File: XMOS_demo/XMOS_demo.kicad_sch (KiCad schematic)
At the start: 13 parts

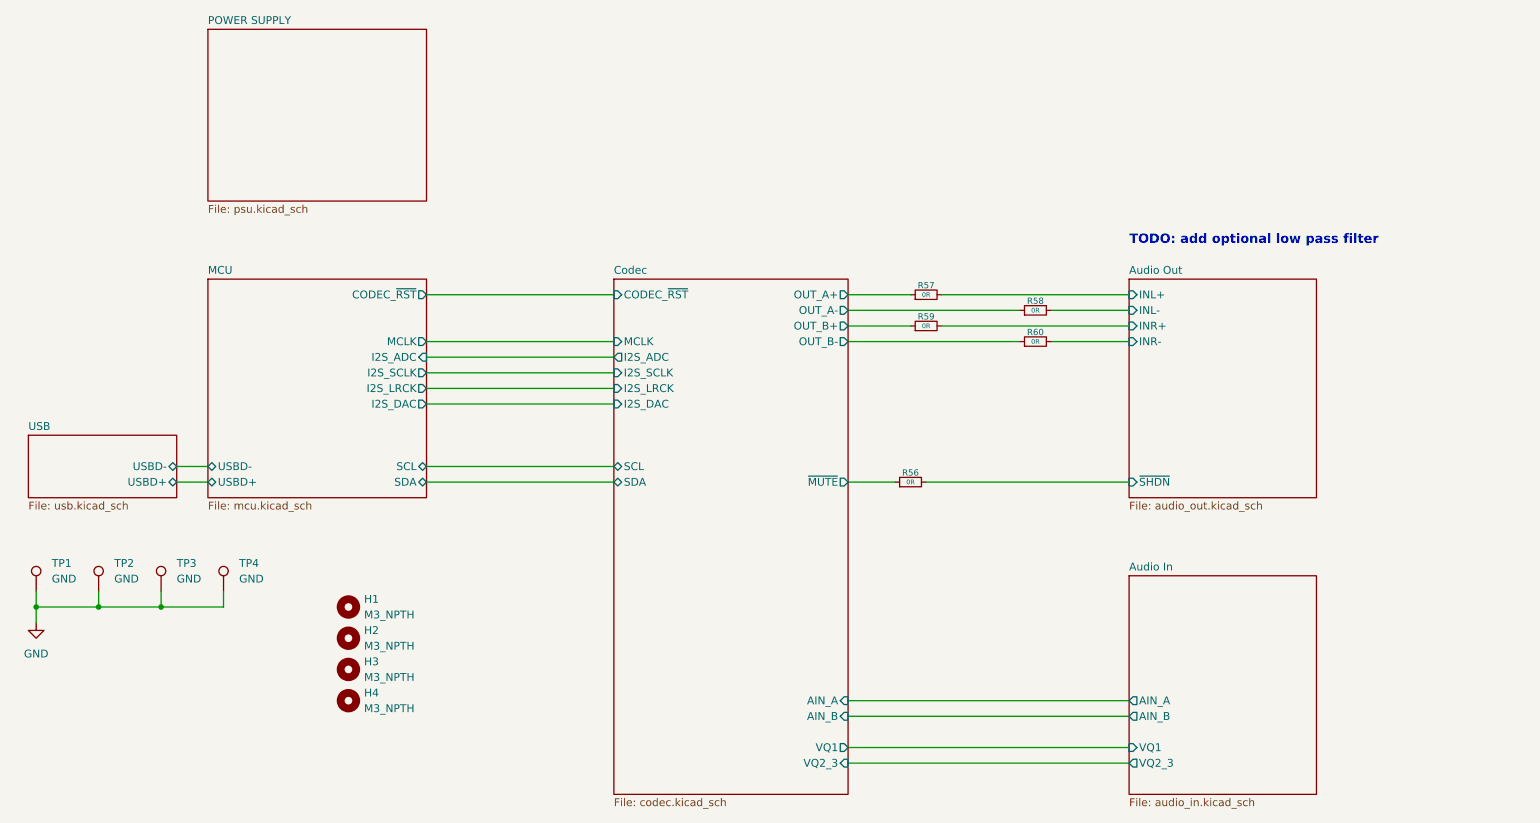
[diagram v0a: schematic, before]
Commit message: I2S config sch page added
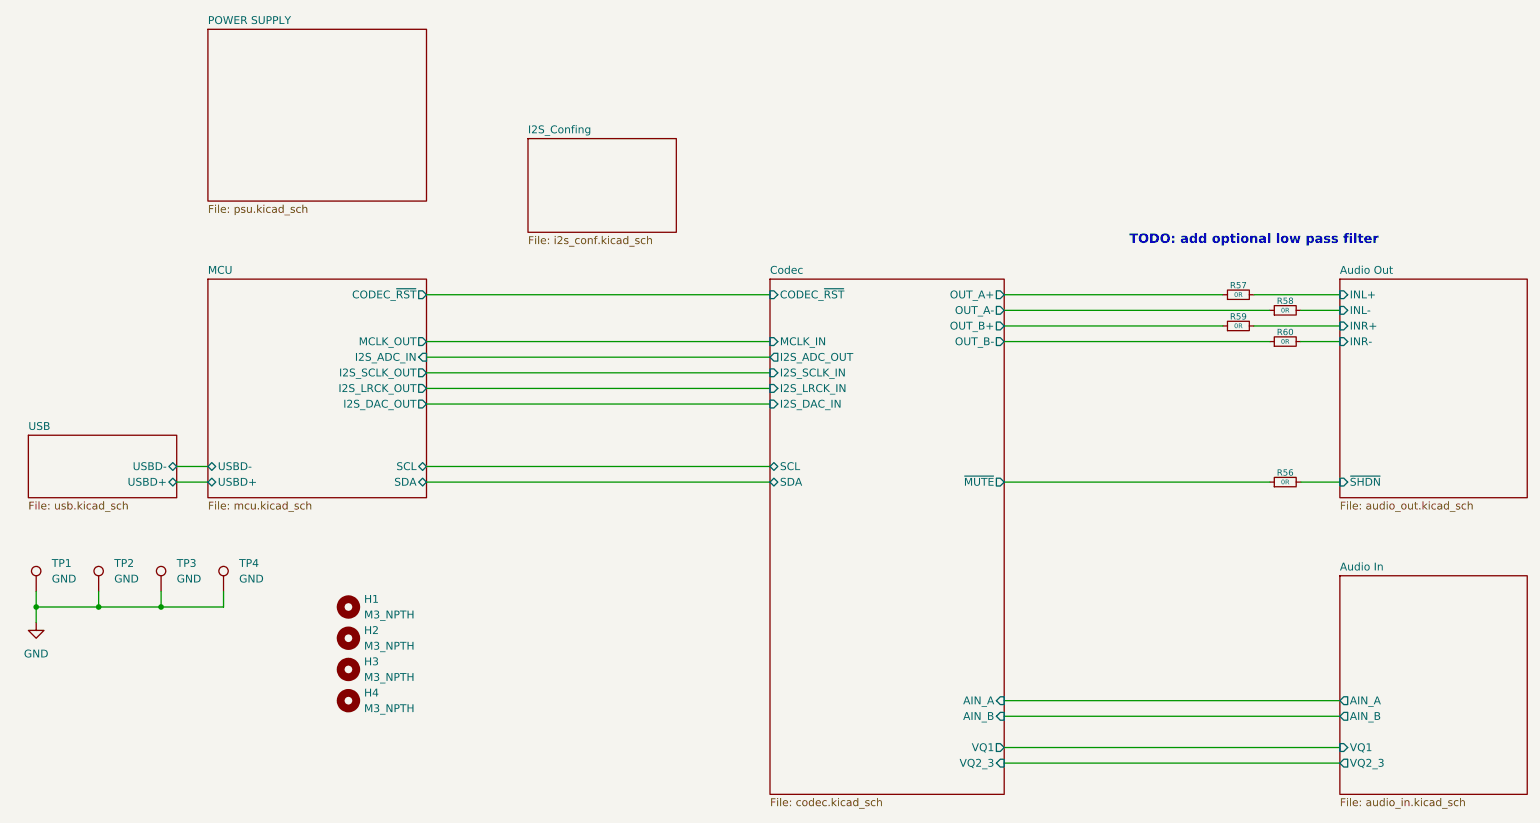
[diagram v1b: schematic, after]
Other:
- added sheet I2S_Confing (i2s_conf.kicad_sch)
- sheet Codec ports: added I2S_ADC_OUT, I2S_DAC_IN, I2S_LRCK_IN, I2S_SCLK_IN, MCLK_IN; removed I2S_ADC, I2S_DAC, I2S_LRCK, I2S_SCLK, MCLK
- sheet MCU ports: added I2S_ADC_IN, I2S_DAC_OUT, I2S_LRCK_OUT, I2S_SCLK_OUT, MCLK_OUT; removed I2S_ADC, I2S_DAC, I2S_LRCK, I2S_SCLK, MCLK
- moved on the sheet: R56, R57, R58, R59, R60

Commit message: Summary (required)
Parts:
- renumbered R57 to R1, R58 to R2, R59 to R3, R60 to R4, R56 to R5
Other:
- sheet I2S_Confing ports: added I2S_ADC_IN, I2S_ADC_OUT, I2S_DAC_IN, I2S_DAC_OUT, I2S_LRCK_IN, I2S_LRCK_OUT, I2S_SCLK_IN, I2S_SCLK_OUT, MCLK_IN, MCLK_OUT; removed none

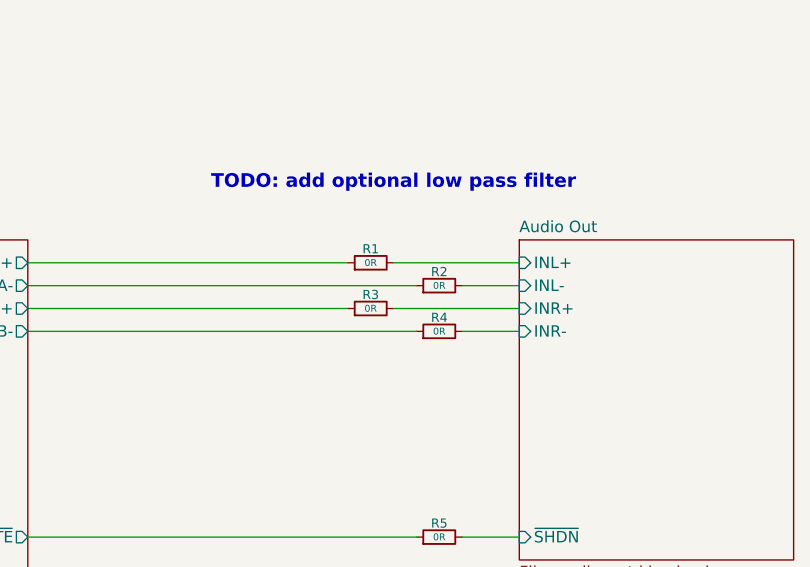
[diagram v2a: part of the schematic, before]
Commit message: Started changes on power supply (audio in) on schematic
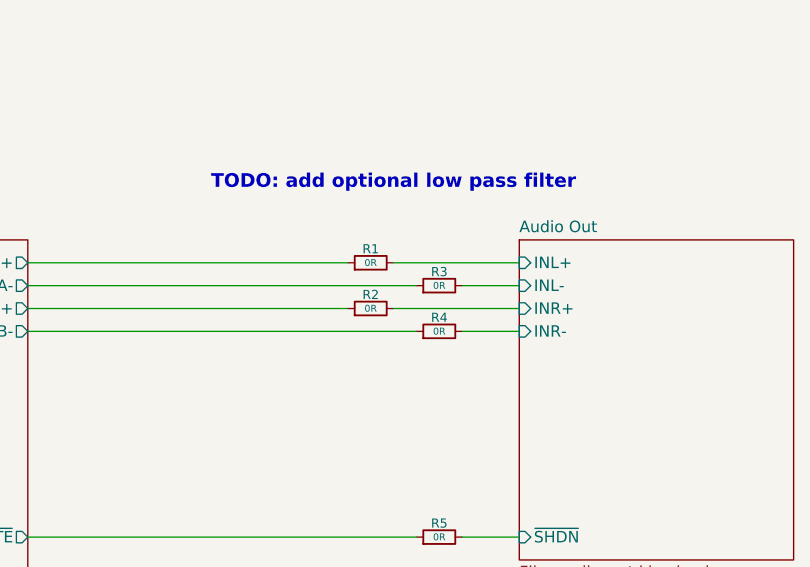
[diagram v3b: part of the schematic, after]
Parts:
- renumbered R3 to R2, R2 to R3
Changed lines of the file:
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@@
 		(on_board yes)
 		(dnp no)
-		(property "Reference" "R3"
+		(property "Reference" "R2"
 			(at 231.14 82.296 90)
 			(effects
@@
 			(project "XMOS_demo"
 				(path "/0a855fb0-ca19-4770-811e-70d8770d7fdd"
-					(reference "R3")
+					(reference "R2")
 					(unit 1)
 				)
@@
 		(on_board yes)
 		(dnp no)
-		(property "Reference" "R2"
+		(property "Reference" "R3"
 			(at 238.76 79.756 90)
 			(effects
@@
 			(project "XMOS_demo"
 				(path "/0a855fb0-ca19-4770-811e-70d8770d7fdd"
-					(reference "R2")
-					(unit 1)
-				)
+					(reference "R3")
+					(unit 1)
+				)

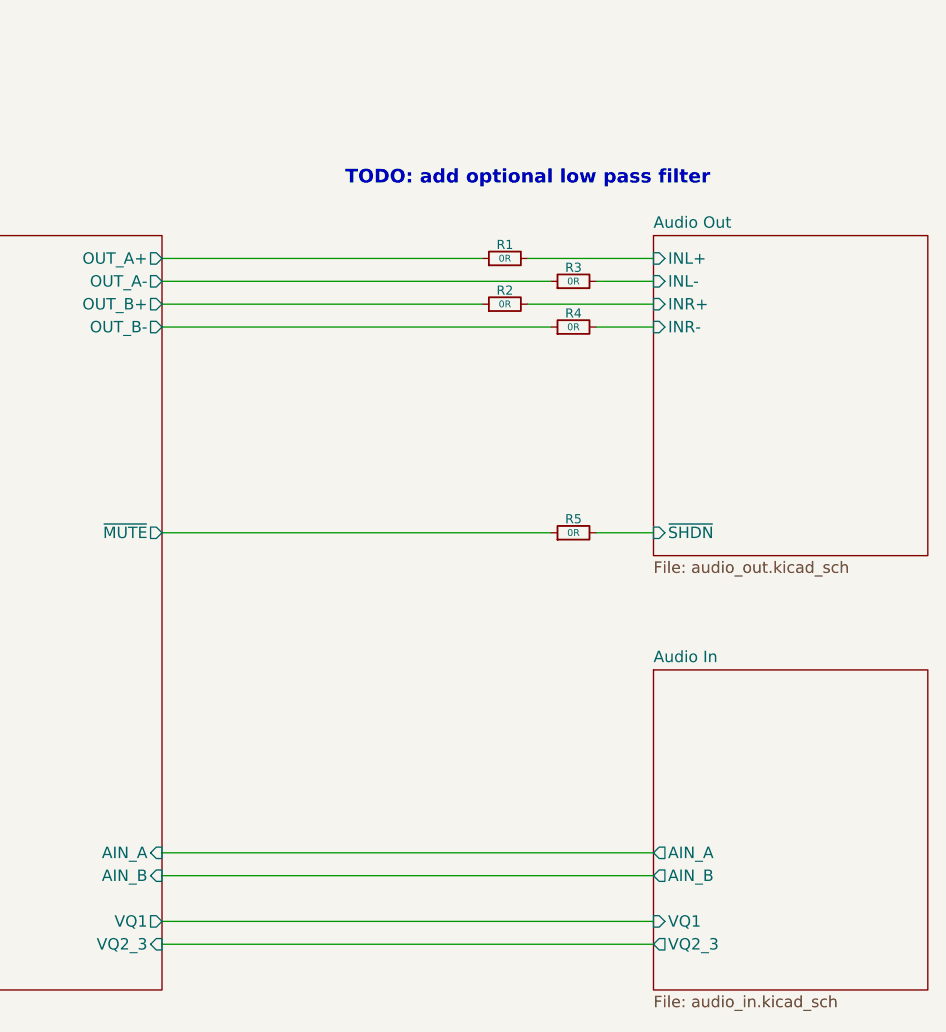
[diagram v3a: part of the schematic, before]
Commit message: Passive lpf added to autio output
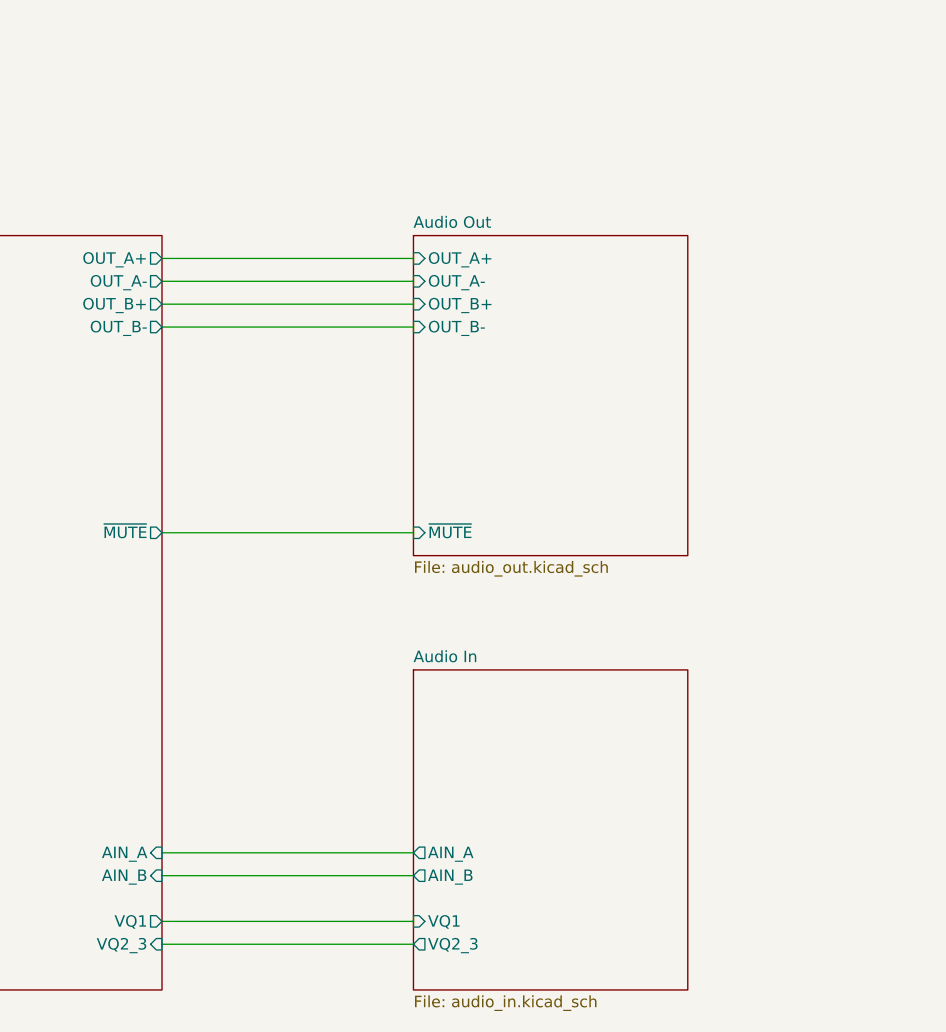
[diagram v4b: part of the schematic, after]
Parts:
- removed R1, R2, R3, R4, R5: 0R, Resistor_SMD:R_0603_1608Metric, symbol Device:R_Small
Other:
- sheet Audio Out ports: added OUT_A+, OUT_A-, OUT_B+, OUT_B-, ~{MUTE}; removed INL+, INL-, INR+, INR-, ~{SHDN}
- note removed: "TODO: add optional low pass filter"
